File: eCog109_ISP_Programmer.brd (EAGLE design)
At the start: 47.5 x 28 mm, 3 parts

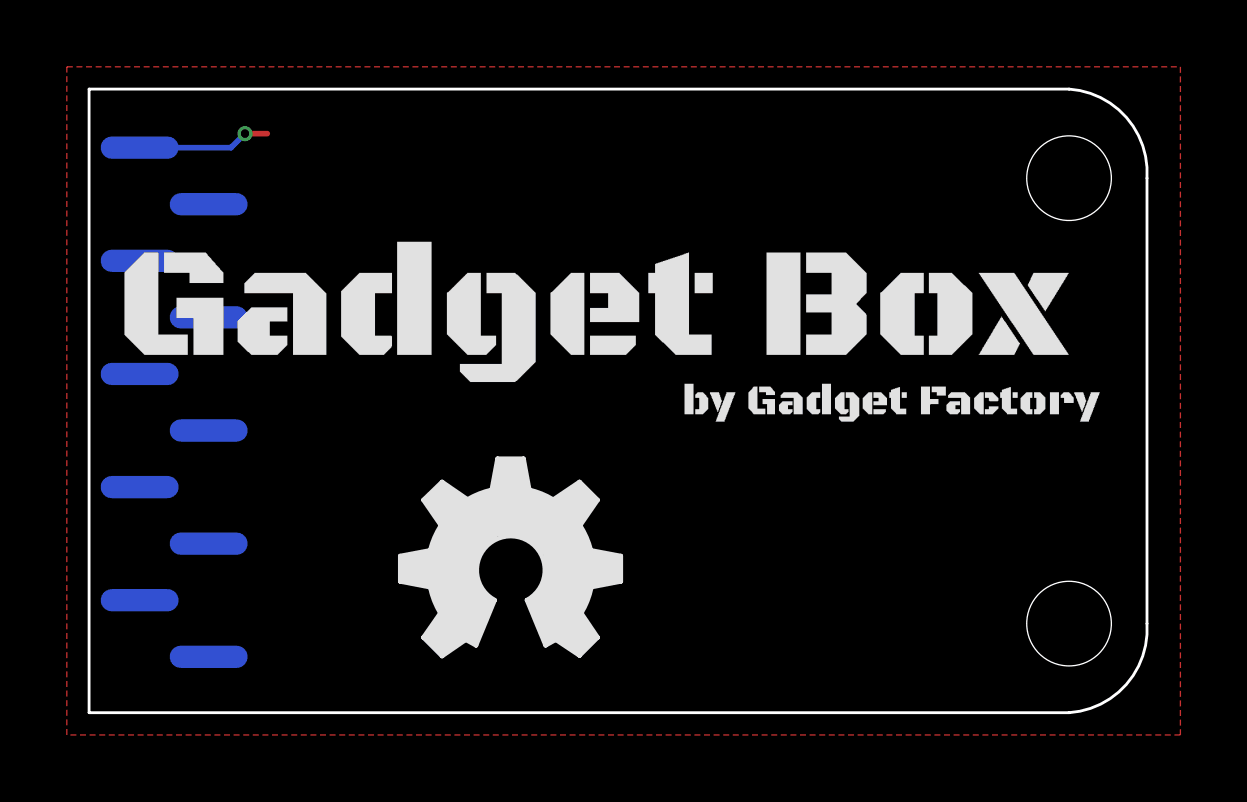
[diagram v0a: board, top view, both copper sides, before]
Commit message: Added new eCogs
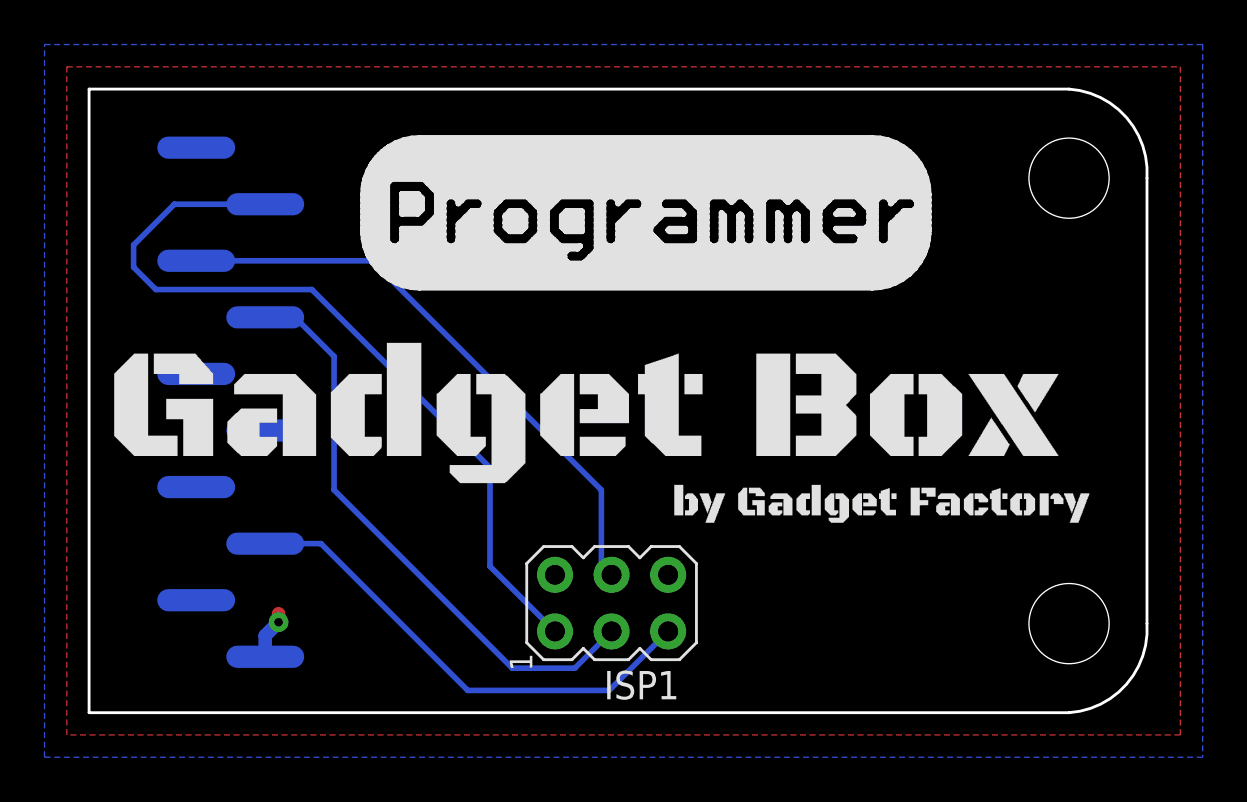
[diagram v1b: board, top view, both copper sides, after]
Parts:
- removed U$2: (no value), GadgetFactory:GADGETBOX_TEXT
- added ISP1: AVRISP-6, adafruit:AVRISP
- ECOG: value ECOG_GENERAL_ROWECOG_GENERAL_SMD -> ECOG_BUSES_ROWECOG_BUSES_SMD; device eCogs:ECOG_GENERAL_SMD -> eCogs:ECOG_BUSES_SMD
- U$1: device ohw-logo:OSHW_FILLX350_NOTEXT -> GadgetFactory:GADGETBOX_TEXT
- moved U$1 13.6 mm to (22.4, 13.2)
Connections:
- new net N$1: ECOG.SPI-MISO, ISP1.1
- new net N$2: ECOG.SPI-SCK, ISP1.3
- new net N$3: ECOG.RESET, ISP1.5
- new net N$4: ECOG.SPI-MOSI, ISP1.4
- net 3V3: now also ISP1.2
- net GND: now also ISP1.6
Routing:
- net N$1: track 0.00 -> 36.0 mm
- net N$4: track 0.00 -> 26.5 mm
- net N$2: track 0.00 -> 26.3 mm
- net N$3: track 0.00 -> 21.9 mm
- net GND: track 5.99 -> 0.00 mm, vias 1 -> 0
- net 3V3: track 0.00 -> 2.18 mm, vias 0 -> 1
- added copper zone on layer 1, net 3V3
- added copper zone on layer 16, net GND
- removed copper zone on layer 1, net GND
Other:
- board text added: "3.3V"
- board text added: "5V"
- board text added: "GND"
- board text added: "ISP Programmer"
- board text added: "RESET"
- board text added: "SPI-MOSI<"
- board text added: "SPI-MOSI>"
- board text added: "SPI-SCK>"
- board text added: "ecog109 v1.0"
- board text added: "ecog109.GadgetFactory.net"
- board text removed: "Blank"
- board text removed: "ecog0 v1.5"
- board text removed: "ecog0.GadgetFactory.net"
